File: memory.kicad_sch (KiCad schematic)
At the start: 7 parts, among them J3 1042240820, U2 MFF2-SIM, U3 24AA01T-I/OT

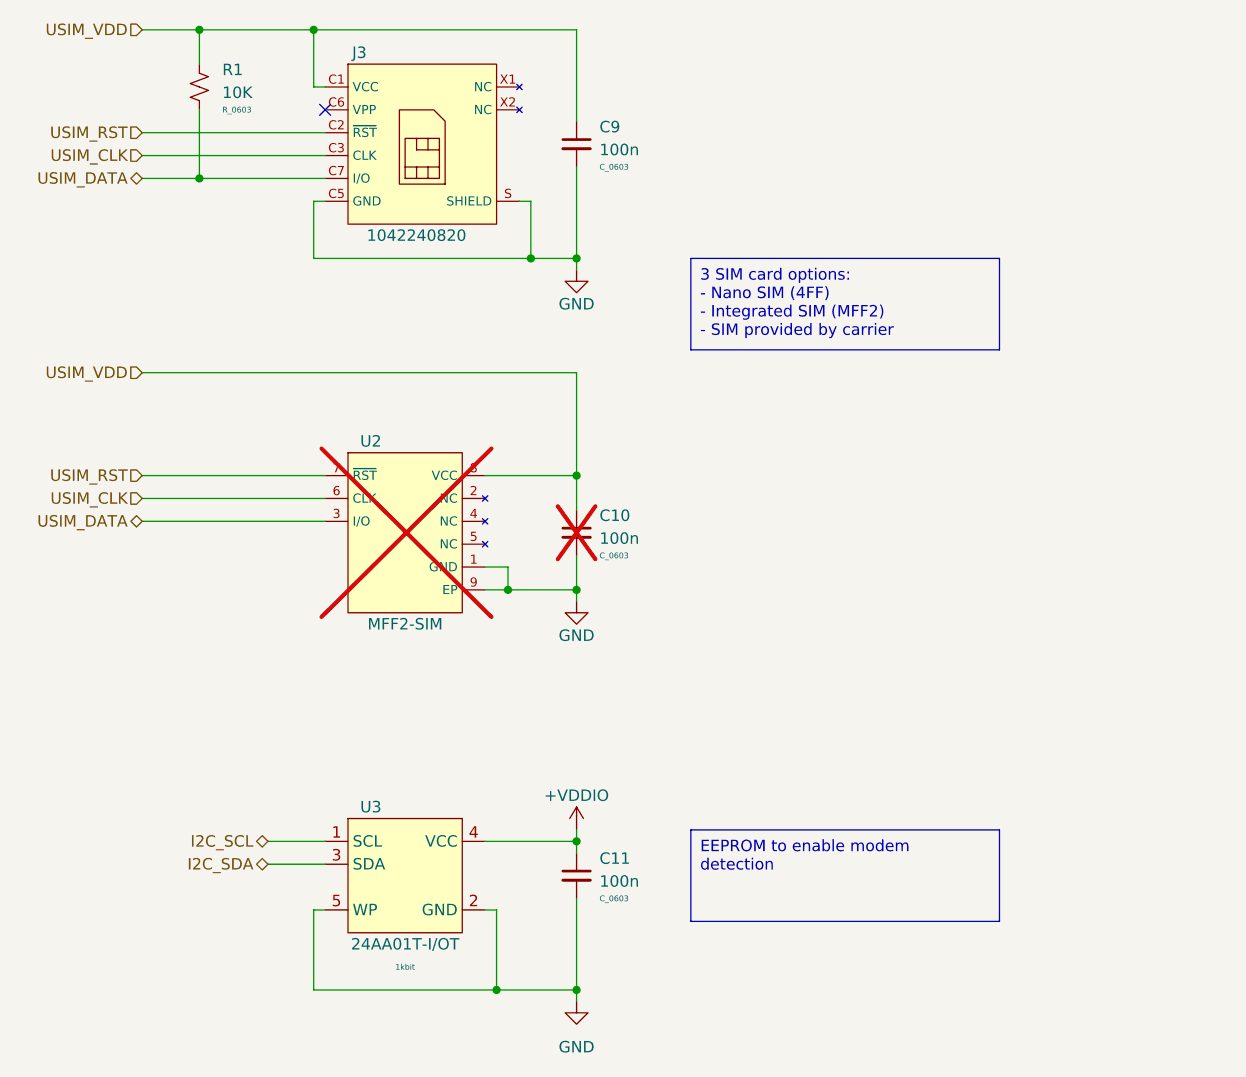
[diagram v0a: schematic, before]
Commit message: Remove PON_TRIG key, add PWRKEY control.
Remove USIM options on PCIE interface.
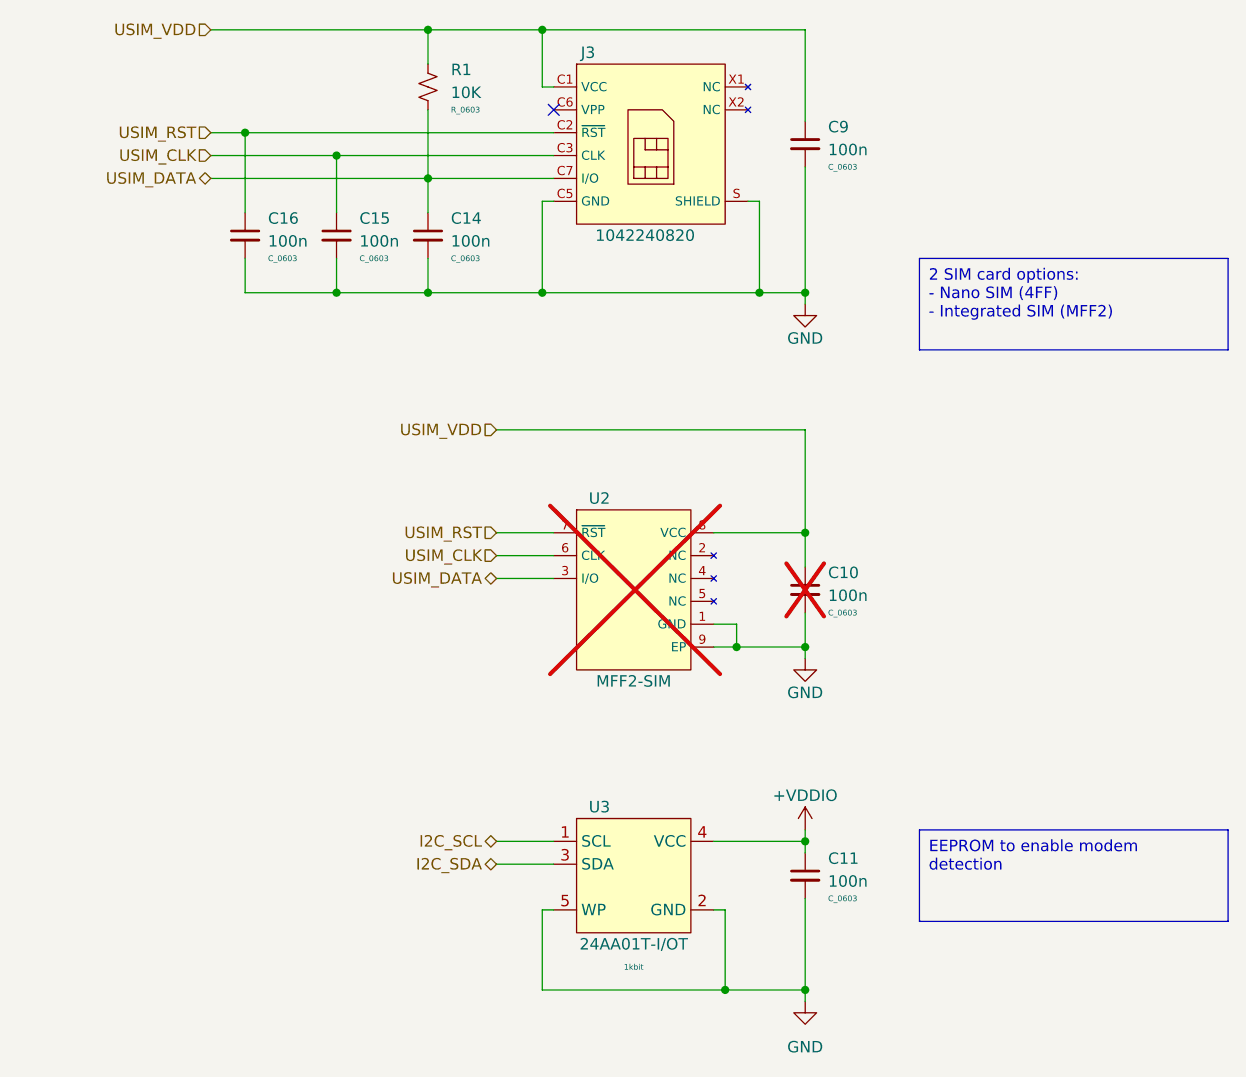
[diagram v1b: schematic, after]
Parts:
- added C14, C15, C16: 100n, C_Capacitor:C_0603, symbol C_Capacitor:C_0603
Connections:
- net GND: now also C14.2, C15.2, C16.2
- net USIM_CLK: now also C15.1
- net USIM_DATA: now also C14.1
- net USIM_RST: now also C16.1
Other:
- moved on the sheet: C10, C11, C9, J3, R1, U2, U3

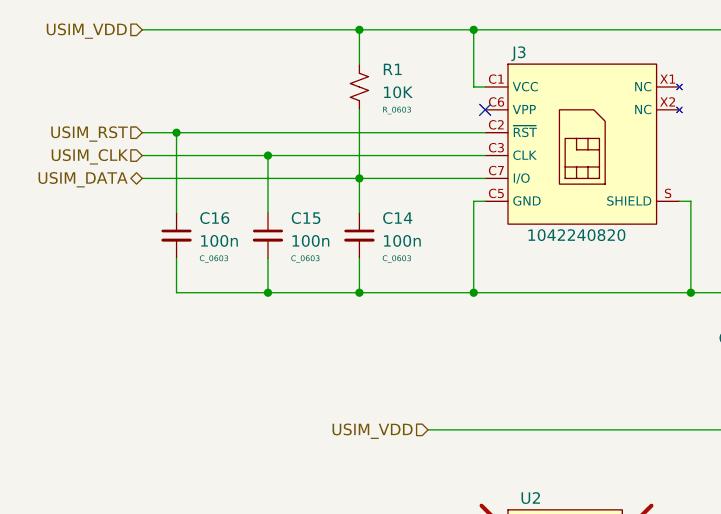
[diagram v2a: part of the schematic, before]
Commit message: Fix 33p caps
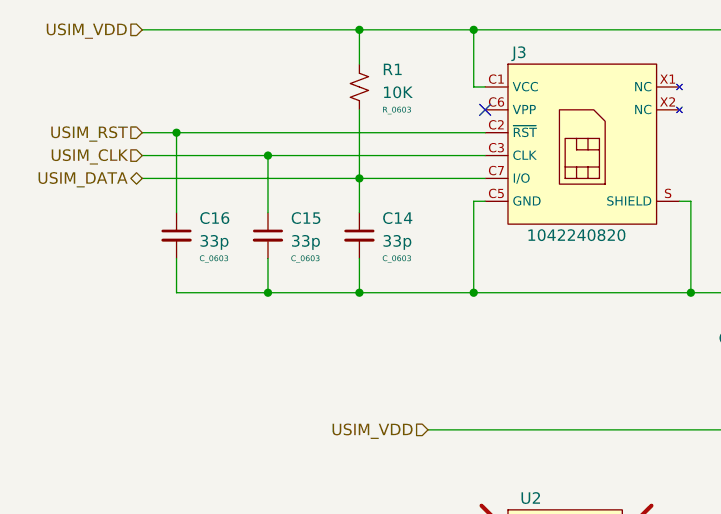
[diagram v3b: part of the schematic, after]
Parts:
- C14, C15, C16: value 100n -> 33p
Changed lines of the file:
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@@
 		(fields_autoplaced yes)
 		(property "Reference" "C15"
-			(at 77.47 59.0613 0)
-			(effects
-				(font
-					(size 1.27 1.27)
-				)
-				(justify left)
-			)
-		)
-		(property "Value" "100n"
-			(at 77.47 61.6013 0)
+			(at 77.47 59.0612 0)
+			(effects
+				(font
+					(size 1.27 1.27)
+				)
+				(justify left)
+			)
+		)
+		(property "Value" "33p"
+			(at 77.47 61.6012 0)
 			(effects
 				(font
@@
 		(fields_autoplaced yes)
 		(property "Reference" "C16"
-			(at 67.31 59.0613 0)
-			(effects
-				(font
-					(size 1.27 1.27)
-				)
-				(justify left)
-			)
-		)
-		(property "Value" "100n"
-			(at 67.31 61.6013 0)
+			(at 67.31 59.0612 0)
+			(effects
+				(font
+					(size 1.27 1.27)
+				)
+				(justify left)
+			)
+		)
+		(property "Value" "33p"
+			(at 67.31 61.6012 0)
 			(effects
 				(font
@@
 		(fields_autoplaced yes)
 		(property "Reference" "C14"
-			(at 87.63 59.0613 0)
-			(effects
-				(font
-					(size 1.27 1.27)
-				)
-				(justify left)
-			)
-		)
-		(property "Value" "100n"
-			(at 87.63 61.6013 0)
-			(effects
-				(font
+			(at 87.63 59.0612 0)
+			(effects
+				(font
+					(size 1.27 1.27)
+				)
+				(justify left)
+			)
+		)
+		(property "Value" "33p"
+			(at 87.63 61.6012 0)
+			(effects
+				(font

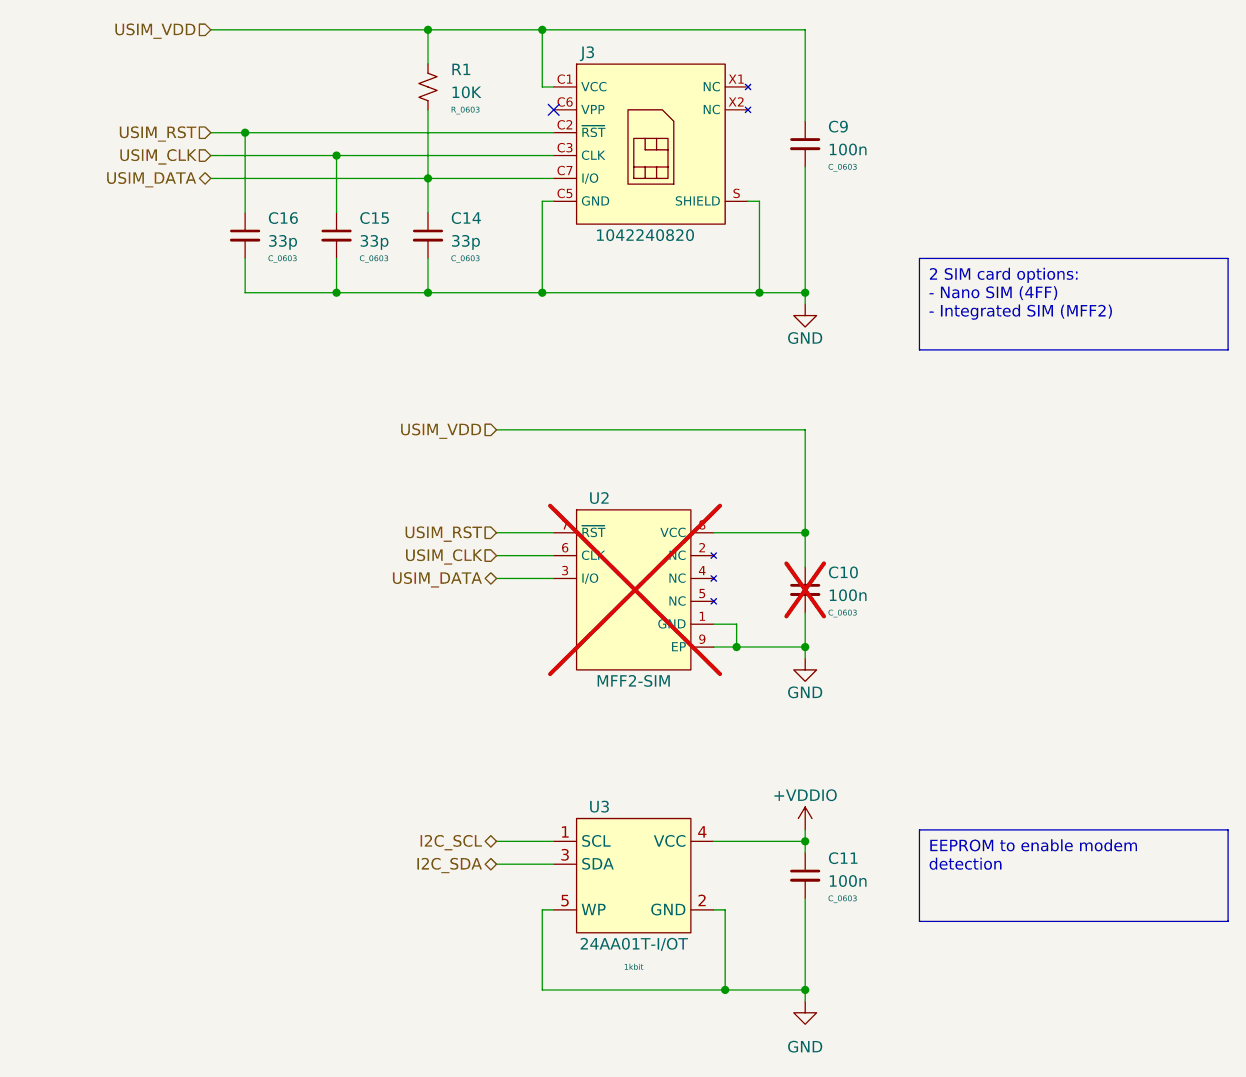
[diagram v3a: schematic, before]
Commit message: Implement fixes
Closes #2
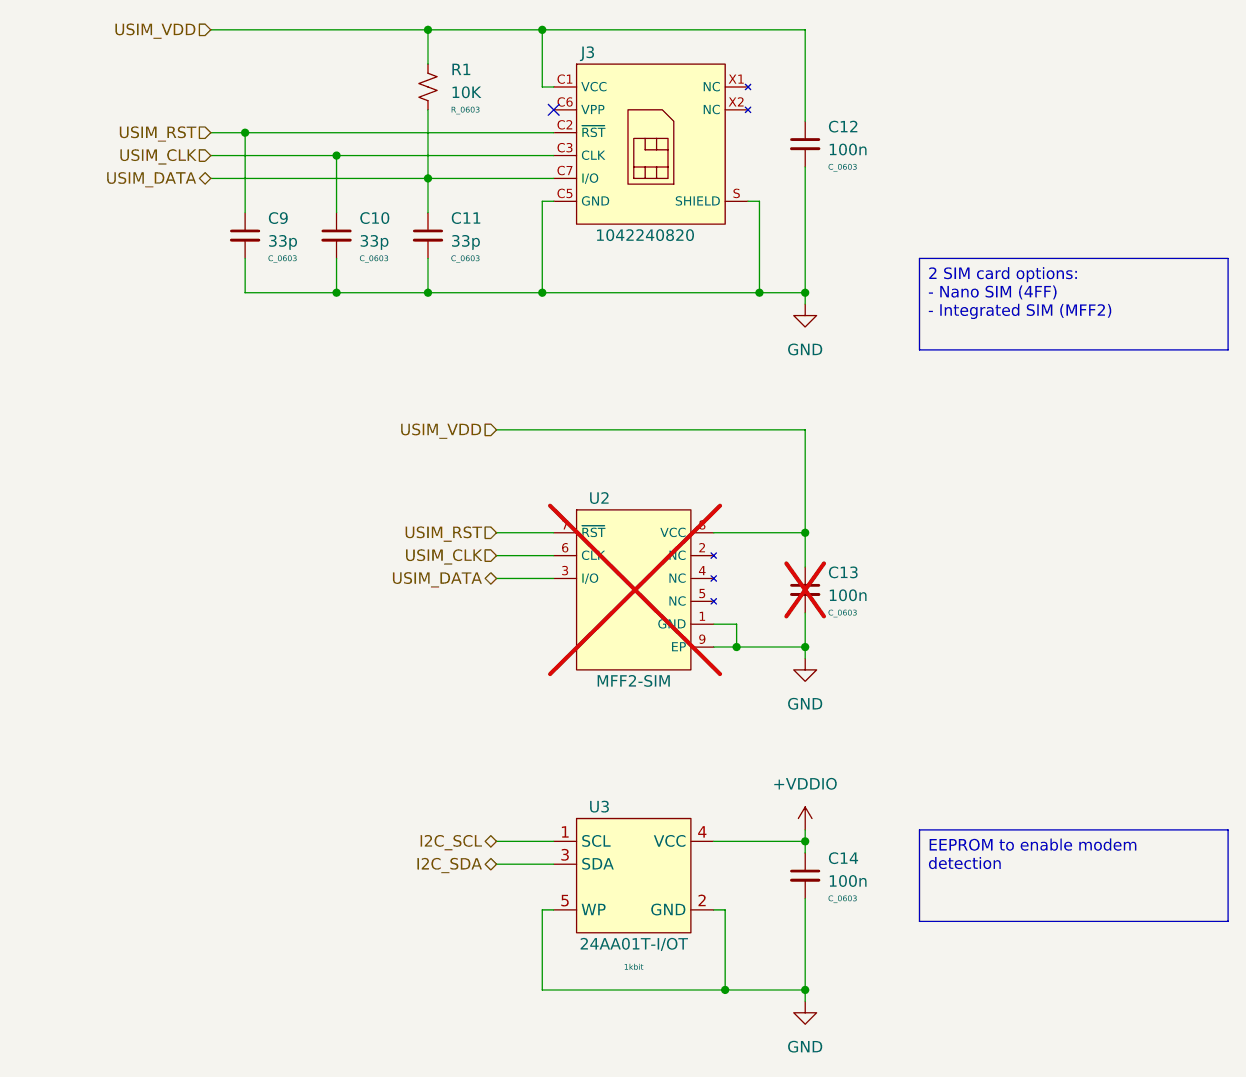
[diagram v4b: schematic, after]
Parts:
- renumbered C15 to C10, C14 to C11, C9 to C12, C10 to C13, C11 to C14, C16 to C9
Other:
- company: (none) -> TL Embedded
- title: (none) -> Winglet BG95

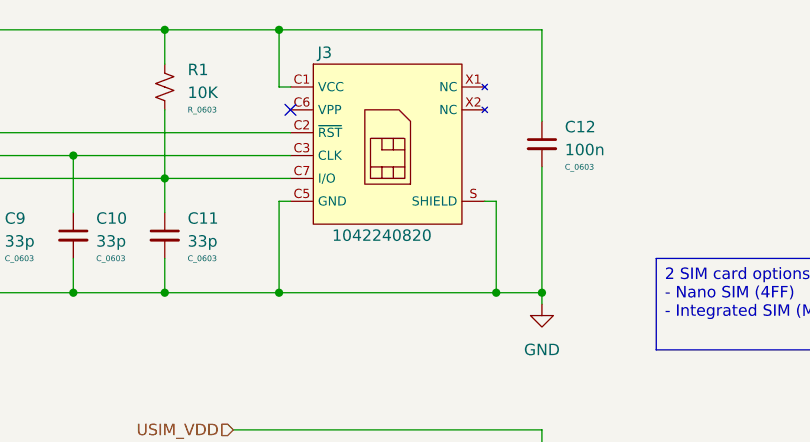
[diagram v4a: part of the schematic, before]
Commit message: Move to NSIM-16-B sim card holder for easier sourcing
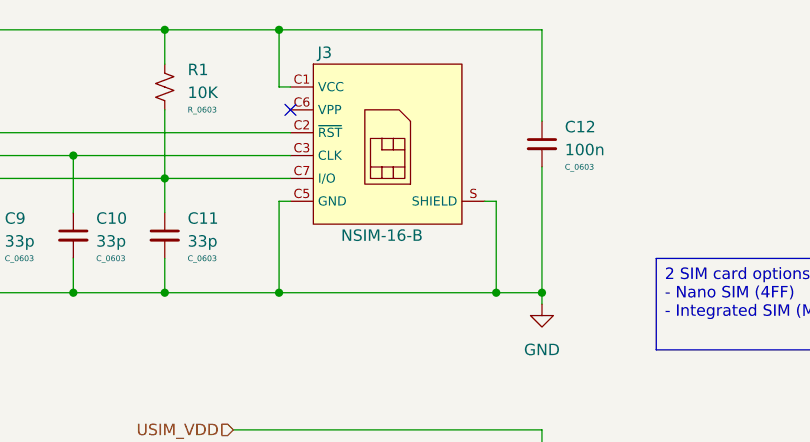
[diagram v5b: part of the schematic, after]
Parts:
- removed J3: 1042240820, J_Connector:1042240820, symbol J_Connector:1042240820
- added J3: NSIM-16-B, J_Connector:NSIM-16-B, symbol J_Connector:NSIM-16-B
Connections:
- net GND: now also J3.C5 (GND), J3.S (SHIELD)
- net USIM_CLK: now also J3.C3 (CLK)
- net USIM_DATA: now also J3.C7 (I/O)
- net USIM_RST: now also J3.C2 (~{RST})
- net USIM_VDD: now also J3.C1 (VCC)
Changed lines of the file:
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@@
+	)
+	(symbol
+		(lib_id "J_Connector:NSIM-16-B")
+		(at 101.6 59.69 0)
+		(unit 1)
+		(exclude_from_sim no)
+		(in_bom yes)
+		(on_board yes)
+		(dnp no)
+		(property "Reference" "J3"
+			(at 102.87 40.64 0)
+			(effects
+				(font
+					(size 1.27 1.27)
+				)
+			)
+		)
+		(property "Value" "NSIM-16-B"
+			(at 109.22 60.96 0)
+			(effects
+				(font
+					(size 1.27 1.27)
+				)
+			)
+		)
+		(property "Footprint" "J_Connector:NSIM-16-B"
+			(at 110.49 66.04 0)
+			(effects
+				(font
+					(size 1.27 1.27)
+				)
+				(hide yes)
+			)
+		)
+		(property "Datasheet" "https://www.sameskydevices.com/product/resource/digikeypdf/nsim-16-b.pdf"
+			(at 99.06 63.5 0)
+			(effects
+				(font
+					(size 1.27 1.27)
+				)
+				(hide yes)
+			)
+		)
+		(property "Description" "CARD CONNECTOR, NANO SIM, PUSH I"
+			(at 109.474 68.58 0)
+			(effects
+				(font
+					(size 1.27 1.27)
+				)
+				(hide yes)
+			)
+		)
+		(pin "S"
+		)
+		(pin "C2"
+		)
+		(pin "C6"
+		)
+		(pin "C1"
+		)
+		(pin "C3"
+		)
+		(pin "C5"
+		)
+		(pin "C7"
+		)
+		(instances
+			(project ""
+				(path "/332623d6-c22a-48da-966b-0d541566aa2d/f3f940f5-dcec-4792-bd6b-0fb823198a56"
+					(reference "J3")
+					(unit 1)
+				)
+			)
+		)
 	)
 	(symbol
@@
 					(unit 1)
 				)
-			)
-		)
-	)
-	(symbol
-		(lib_id "J_Connector:1042240820")
-		(at 101.6 59.69 0)
-		(unit 1)
-		(exclude_from_sim no)
-		(in_bom yes)
-		(on_board yes)
-		(dnp no)
-		(property "Reference" "J3"
-			(at 102.87 40.64 0)
-			(effects
-				(font
-					(size 1.27 1.27)
-				)
-			)
-		)
-		(property "Value" "1042240820"
-			(at 109.22 60.96 0)
-			(effects
-				(font
-					(size 1.27 1.27)
-				)
-			)
-		)
-		(property "Footprint" "J_Connector:1042240820"
-			(at 110.49 66.04 0)
-			(effects
-				(font
-					(size 1.27 1.27)
-				)
-				(hide yes)
-			)
-		)
-		(property "Datasheet" "https://www.molex.com/content/dam/molex/molex-dot-com/products/automated/en-us/salesdrawingpdf/104/104224/1042240820_sd.pdf"
-			(at 99.695 63.5 0)
-			(effects
-				(font
-					(size 1.27 1.27)
-				)
-				(hide yes)
-			)
-		)
-		(property "Description" "NANOSIM SOCKET 1.11H P/PULL TYPE"
-			(at 101.6 59.69 0)
-			(effects
-				(font
-					(size 1.27 1.27)
-				)
-				(hide yes)
-			)
-		)
-		(pin "C1"
-		)
-		(pin "C2"
-		)
-		(pin "C3"
-		)
-		(pin "C5"
-		)
-		(pin "C6"
-		)
-		(pin "C7"
-		)
-		(pin "S"
-		)
-		(pin "X1"
-		)
-		(pin "X2"
-		)
-		(instances
-			(project "Winglet-BG95"
-				(path "/332623d6-c22a-48da-966b-0d541566aa2d/f3f940f5-dcec-4792-bd6b-0fb823198a56"
-					(reference "J3")
-					(unit 1)
-				)
